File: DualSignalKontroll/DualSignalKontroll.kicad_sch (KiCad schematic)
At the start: 44 parts, among them J6 Screw_Terminal_01x05, J7 Screw_Terminal_01x05, Q1 BC547, Q2 BC547, Q3 BC547, Q4 BC547, Q5 BC547, Q6 BC547, U1 L7805, U2 PC817, U3 PC817, U4 PC817, U5 PC817, U6 PC817

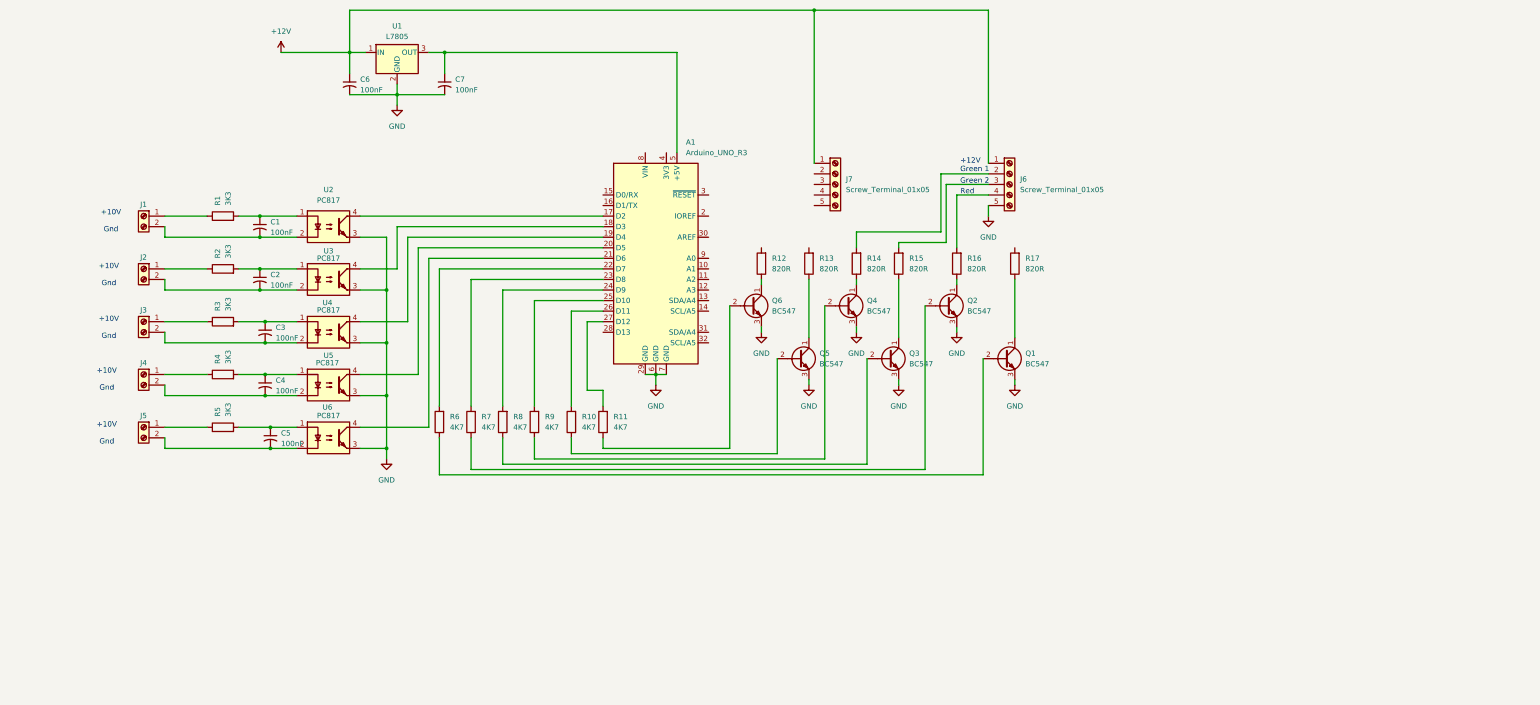
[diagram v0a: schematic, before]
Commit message: Added EEPROM
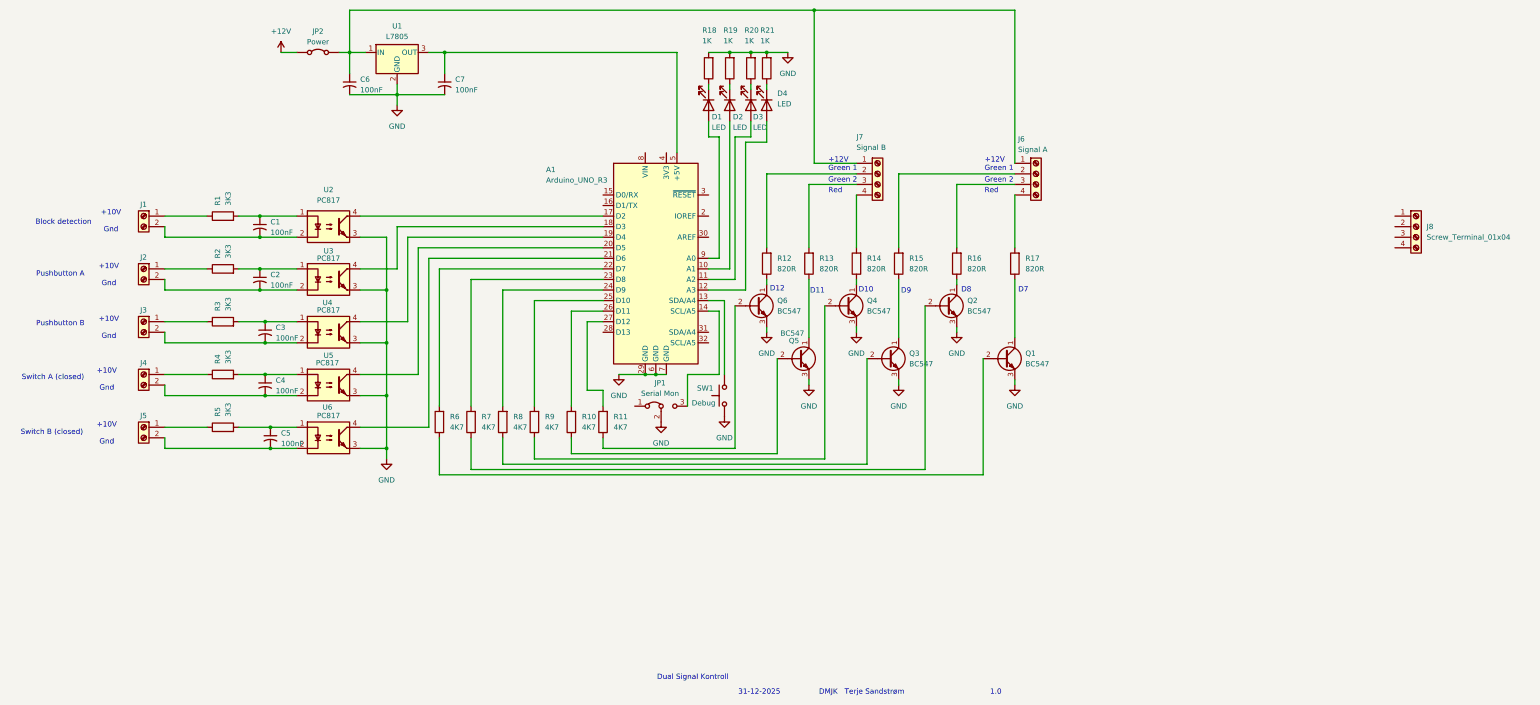
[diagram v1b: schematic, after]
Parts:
- removed J6, J7: Screw_Terminal_01x05, symbol Connector:Screw_Terminal_01x05
- added D1, D2, D3, D4: LED, symbol Device:LED
- added J6: Signal A, symbol Connector:Screw_Terminal_01x04
- added J7: Signal B, symbol Connector:Screw_Terminal_01x04
- added J8: Screw_Terminal_01x04, symbol Connector:Screw_Terminal_01x04
- added JP1: Serial Mon, symbol Jumper:Jumper_3_Bridged12
- added JP2: Power, symbol Jumper:Jumper_2_Bridged
- added R18, R19, R20, R21: 1K, symbol Device:R
- added SW1: Debug, symbol Switch:SW_Push
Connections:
- net +12V: now also JP2.1 (A); no longer C6.1, U1.1 (IN)
- net GND: now also JP1.2 (C), R18.2, R19.2, R20.2, R21.2, SW1.1
- net at R15.2: now also J6.2 (Pin_2)
- net at R16.2: now also J6.3 (Pin_3)
- net at R17.2: now also J6.4 (Pin_4)
- net at R14.2: now also J7.4 (Pin_4)
- net at R12.2: now also J7.2 (Pin_2)
- net at A1.10 (A1): now also D2.2 (A)
- net at A1.11 (A2): now also D3.2 (A)
- net at A1.12 (A3): now also D4.2 (A)
- net at A1.13 (SDA/A4): now also SW1.2
- net at A1.14 (SCL/A5): now also JP1.3 (B)
- net at A1.9 (A0): now also D1.2 (A)
- net at R13.2: now also J7.3 (Pin_3)
- new net: D1.1 (K), R18.1
- new net: D2.1 (K), R19.1
- new net: C6.1, J6.1 (Pin_1), J7.1 (Pin_1), JP2.2 (B), U1.1 (IN)
- new net: D3.1 (K), R20.1
- new net: D4.1 (K), R21.1
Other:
- note added: "1.0"
- note added: "31-12-2025"
- note added: "Block detection"
- note added: "D10"
- note added: "D11"
- note added: "D12"
- note added: "D7"
- note added: "D8"
- note added: "D9"
- note added: "DMJK Terje Sandstrøm"
- note added: "Dual Signal Kontroll"
- note added: "Pushbutton A"
- note added: "Pushbutton B"
- note added: "Switch A (closed)"
- note added: "Switch B (closed)"
- moved on the sheet: Q6, R12

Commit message: updated schema
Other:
- note added: "A Green"
- note added: "B Green"
- note added: "Direction On: B->A"
- note added: "Train"
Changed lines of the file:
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@@
+		)
+	)
+	(text "A\nGreen"
+		(exclude_from_sim no)
+		(at 210.566 25.146 0)
+		(effects
+			(font
+				(size 1.27 1.27)
+			)
+		)
+	)
+	(text "Train"
+		(exclude_from_sim no)
+		(at 204.724 24.13 0)
+		(effects
+			(font
+				(size 1.27 1.27)
+			)
 		)
 	)
@@
 		)
 	)
+	(text "B\nGreen"
+		(exclude_from_sim no)
+		(at 216.916 25.146 0)
+		(effects
+			(font
+				(size 1.27 1.27)
+			)
+		)
+	)
 	(text "1.0"
 		(exclude_from_sim no)
@@
 		(effects
 			(font
+				(size 1.27 1.27)
+			)
+		)
+	)
+	(text "Direction\nOn: B->A"
+		(exclude_from_sim no)
+		(at 195.834 24.892 0)
+		(effects
+			(font

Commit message: Updated schema and code
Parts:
- added C8: 100nF, symbol Device:C_Small_US
- added D5: 10VZ, Diode_SMD:D_MiniMELF, symbol Diode:BZV55B10
- added J9: Power out, symbol Connector:Screw_Terminal_01x03
- added JP3: 5V, symbol Jumper:Jumper_2_Open
- added JP4: VIN 9V, symbol Jumper:Jumper_2_Open
- added Q7: BD139, Package_TO_SOT_THT:TO-126-3_Vertical, symbol Transistor_BJT:BD139
- added R22: 910R, symbol Device:R
- R1: value 3K3 -> 1K5
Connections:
- net GND: now also C2.2, C3.2, U3.2, U4.2, C8.2, D5.2 (A), J9.3 (Pin_3)
- net at C6.1, J6.1 (Pin_1), J7.1 (Pin_1)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: now also J2.2 (Pin_2), J3.2 (Pin_2), J9.1 (Pin_1), Q7.2 (C), R22.2
- net at C7.1, U1.3 (OUT): now also J9.2 (Pin_2), JP3.1 (A); no longer A1.5 (+5V)
- net at A1.8 (VIN): now also JP4.1 (A)
- new net: D5.1 (K), Q7.3 (B), R22.1
- new net: C8.1, JP4.2 (B), Q7.1 (E)
- new net: A1.5 (+5V), JP3.2 (B)
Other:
- added sheet Connections (Connections.kicad_sch)
- note added: "+5V Gnd"
- note added: "12V 5V Gnd"
- note added: "Input +10V"
- note added: "Input Gnd"
- note added: "Switch A (closed) (10V)"
- note added: "Switch B (closed) (10V)"
- note removed: "+10V Gnd"
- note removed: "Switch A (closed)"
- note removed: "Switch B (closed)"

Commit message: initial code
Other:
- added sheet Untitled Sheet (untitled.kicad_sch)
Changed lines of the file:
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@@
+		)
+	)
+	(sheet
+		(at 33.02 165.735)
+		(size 12.7 3.81)
+		(exclude_from_sim no)
+		(in_bom yes)
+		(on_board yes)
+		(dnp no)
+		(fields_autoplaced yes)
+		(stroke
+			(width 0.1524)
+			(type solid)
+		)
+		(fill
+			(color 0 0 0 0.0000)
+		)
+		(property "Sheetname" "Untitled Sheet"
+			(at 33.02 165.0234 0)
+			(effects
+				(font
+					(size 1.27 1.27)
+				)
+				(justify left bottom)
+			)
+		)
+		(property "Sheetfile" "untitled.kicad_sch"
+			(at 33.02 170.1296 0)
+			(effects
+				(font
+					(size 1.27 1.27)
+				)
+				(justify left top)
+			)
+		)
+		(instances
+			(project "DualSignalKontroll"
+				(path "/f90bb1a2-1a22-420b-b2f2-f9513faf4f93"
+					(page "3")
+				)
+			)
 		)
 	)

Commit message: Started on V2
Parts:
- removed D4: LED, symbol Device:LED
- removed J8: Screw_Terminal_01x04, symbol Connector:Screw_Terminal_01x04
- removed R21: 1K, symbol Device:R
- added C9: 100nF, symbol Device:C_Small_US
- added R23: 3K3, symbol Device:R
- added U7: PC817, Package_DIP:DIP-4_W7.62mm, symbol Isolator:PC817
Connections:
- net GND: now also C1.2, C4.2, C5.2, J1.2 (Pin_2), U2.2, U5.2, U6.2, C9.2, U7.2, U7.3
- net at A1.12 (A3): now also U7.4
- new net: C9.1, R23.2, U7.1
- new net: J5.2 (Pin_2), R23.1
- now unconnected: J4.2 (Pin_2)
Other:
- moved on the sheet: Q5, Q6, R12, R13

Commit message: updated to new V2 code
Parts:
- removed D1, D2, D3: LED, symbol Device:LED
- removed R18, R19, R20: 1K, symbol Device:R
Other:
- removed sheet Untitled Sheet
- note added: "Input B Input CD"
- note added: "Switch C&D (closed) (10V)"
- note removed: "A Green"
- note removed: "B Green"
- note removed: "Direction On: B->A"
- note removed: "Train"

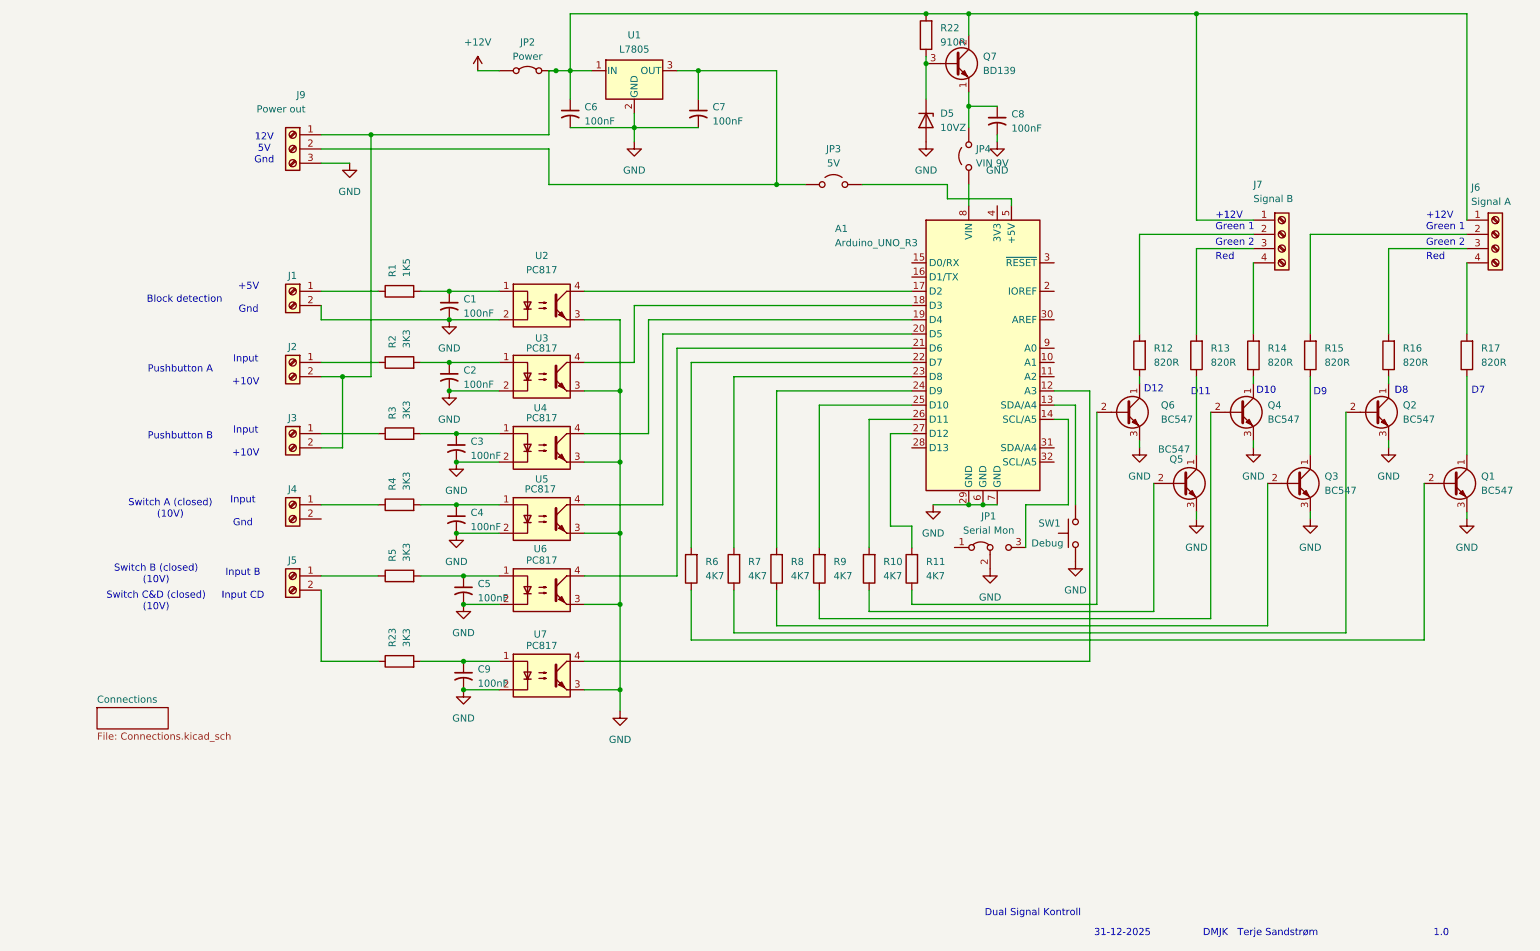
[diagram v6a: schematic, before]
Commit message: Updated schema
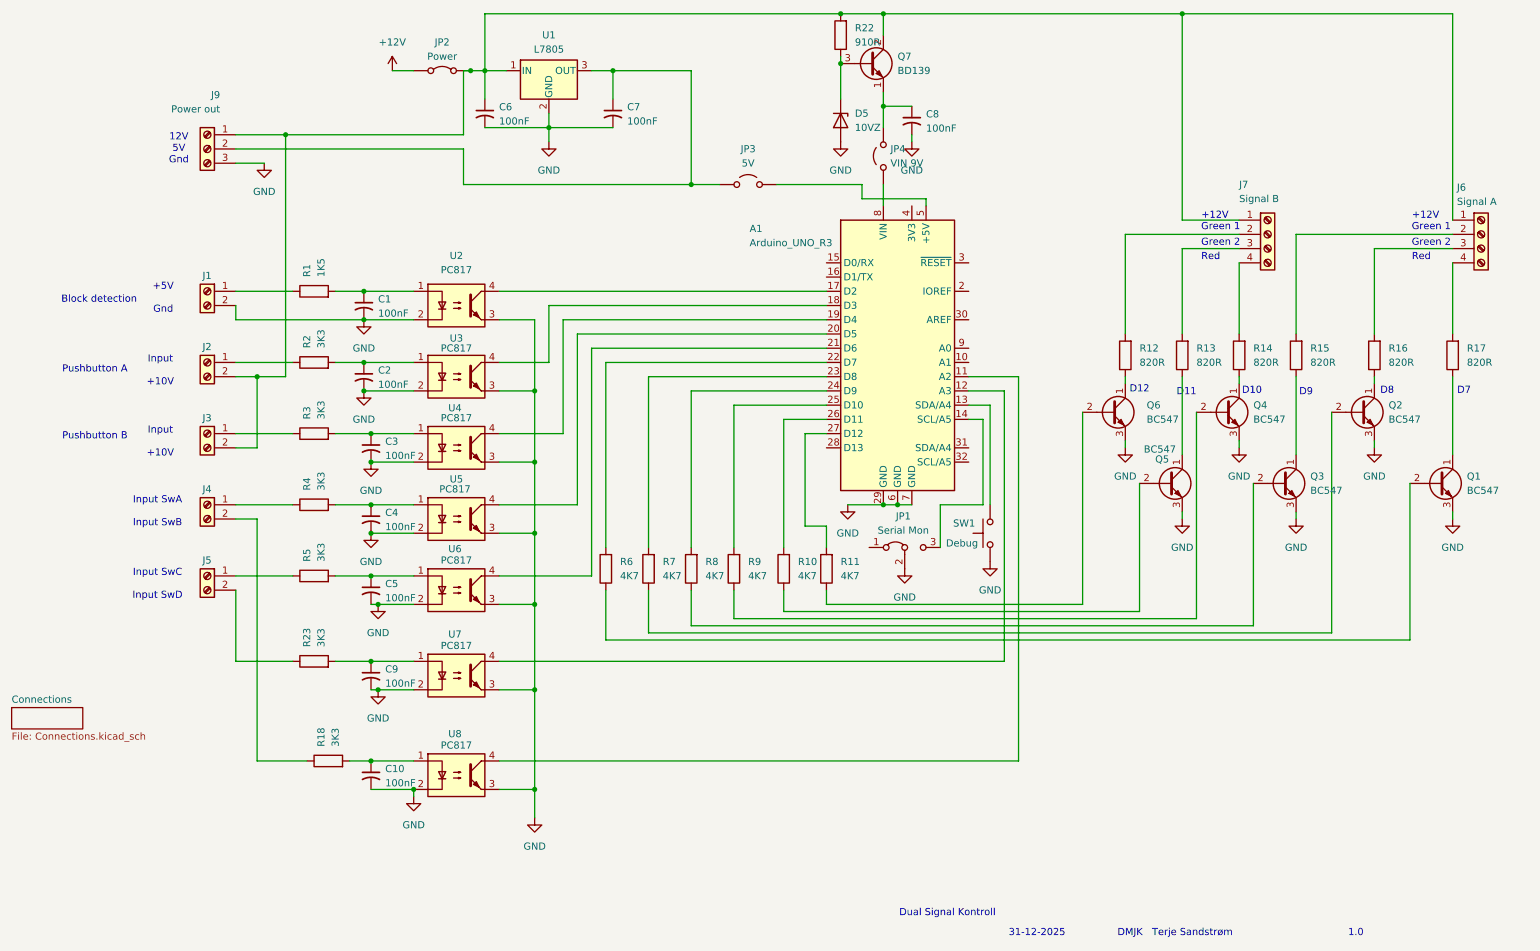
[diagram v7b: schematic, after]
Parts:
- added C10: 100nF, symbol Device:C_Small_US
- added R18: 3K3, symbol Device:R
- added U8: PC817, Package_DIP:DIP-4_W7.62mm, symbol Isolator:PC817
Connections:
- net GND: now also C10.2, U8.2, U8.3
- net at A1.11 (A2): now also U8.4
- net at J4.2 (Pin_2): now also R18.1
- new net: C10.1, R18.2, U8.1
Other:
- note added: "Input SwA Input SwB"
- note added: "Input SwC Input SwD"
- note removed: "Input B Input CD"
- note removed: "Input Gnd"
- note removed: "Switch A (closed) (10V)"
- note removed: "Switch B (closed) (10V)"
- note removed: "Switch C&D (closed) (10V)"
- moved on the sheet: A1, C1, C2, C3, C4, C5, C6, C7, C8, C9, D5, J1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

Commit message: Versjon med 4 penser
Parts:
- added JP5: Direct Conn TrackDetector, symbol Jumper:Jumper_3_Bridged12
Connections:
- net GND: now also C6.1, C7.1, J2.2 (Pin_2), J3.2 (Pin_2), J6.1 (Pin_1), J7.1 (Pin_1), J9.1 (Pin_1), J9.2 (Pin_2), JP2.2 (B), JP3.1 (A), Q7.2 (C), R22.2, U1.1 (IN), U1.3 (OUT)
- net at C1.1, R1.2: now also JP5.2 (C); no longer U2.1
- net at A1.17 (D2), U2.4: now also JP5.3 (B)
- new net: JP5.1 (A), U2.1
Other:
- note added: "Wires to 2nd board"
- moved on the sheet: C1, C2, C3, C4, C5, C9, J1, J2, J3, J4, J5, R1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
